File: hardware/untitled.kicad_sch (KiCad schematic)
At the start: 41 parts, among them J5 DCJ200-10-A-K1-K, J6 USB4105-GF-A, SW1 SW_Push, SW2 SW_Push, U3 NCP1117ST33T3G, U4 ESP32-S3-WROOM-1-N8R8, U5 USBLC6-2SC6

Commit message: SD card routing v0.1
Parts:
- removed R23: 50R, Resistor_SMD:R_0603_1608Metric_Pad0.98x0.95mm_HandSolder, symbol Device:R
- SW1: renamed from S1; footprint R1966ABLKBLKGR -> ESP32-project-footprints:RA1113112R
- renumbered R15 to R17, R16 to R18, R17 to R19, R18 to R20, R19 to R21, R20 to R22, R21 to R23, R22 to R24, R24 to R25, R25 to R26, SW1 to SW2, SW2 to SW3
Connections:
- net +5V: no longer C19.1
- net SPI2_MISO: now also U4.21 (IO13)
- net VBUS: now also C19.1
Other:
- note removed: "NEW SWITCH"
- moved on the sheet: C19, U5

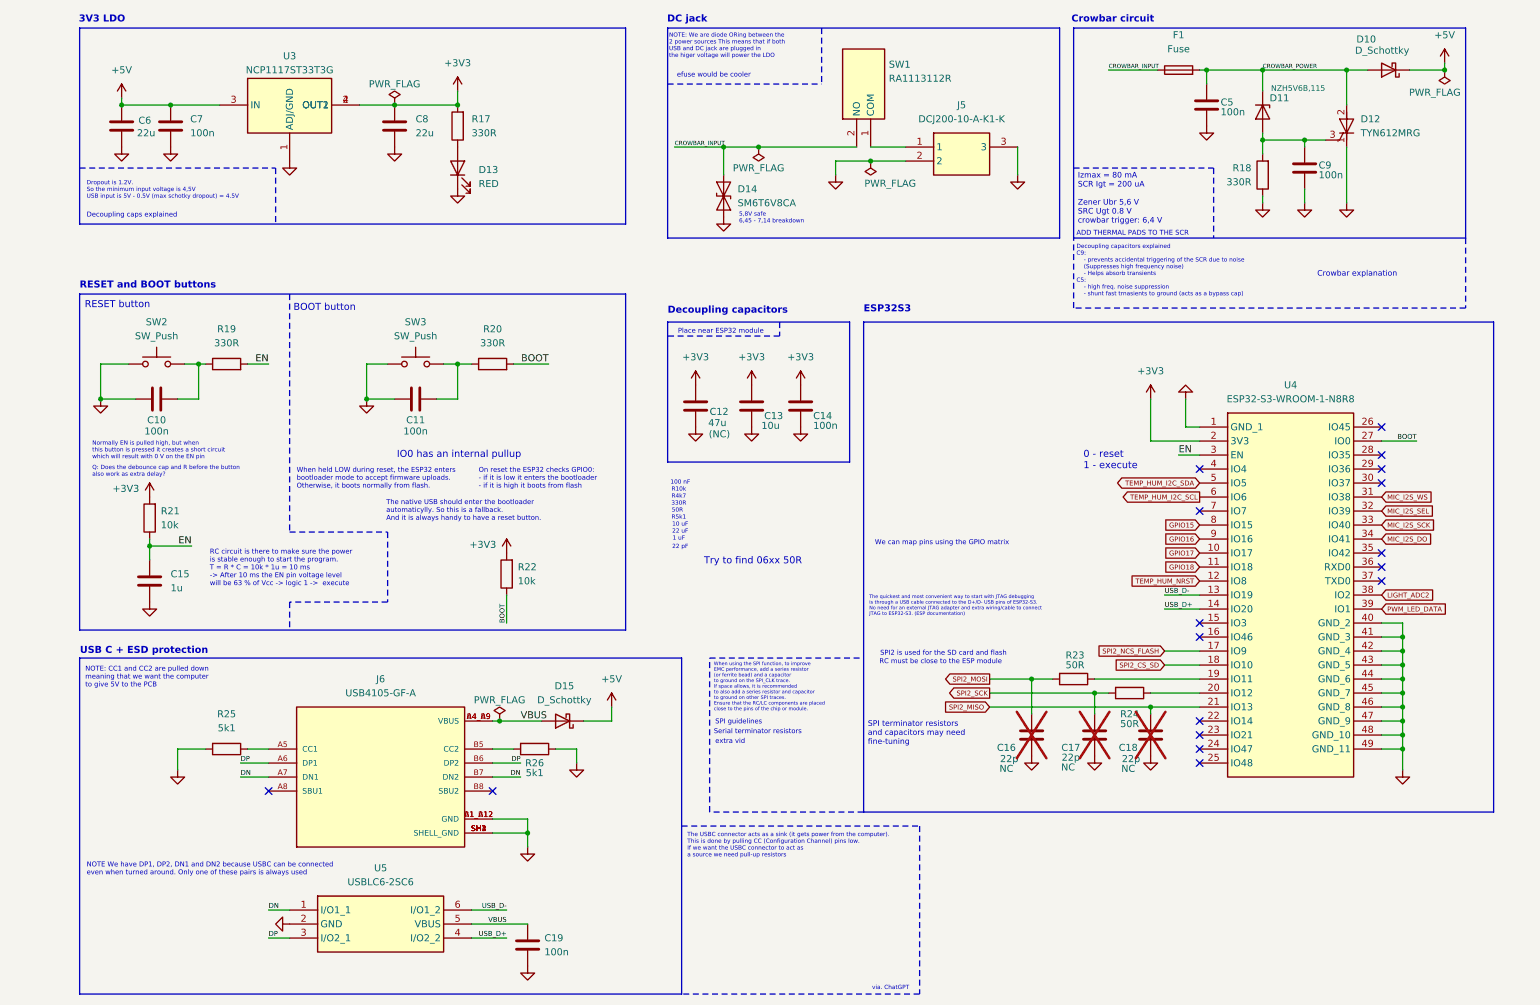
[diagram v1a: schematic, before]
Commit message: v0.3.1 Changed board stackup and impedance controlled traces
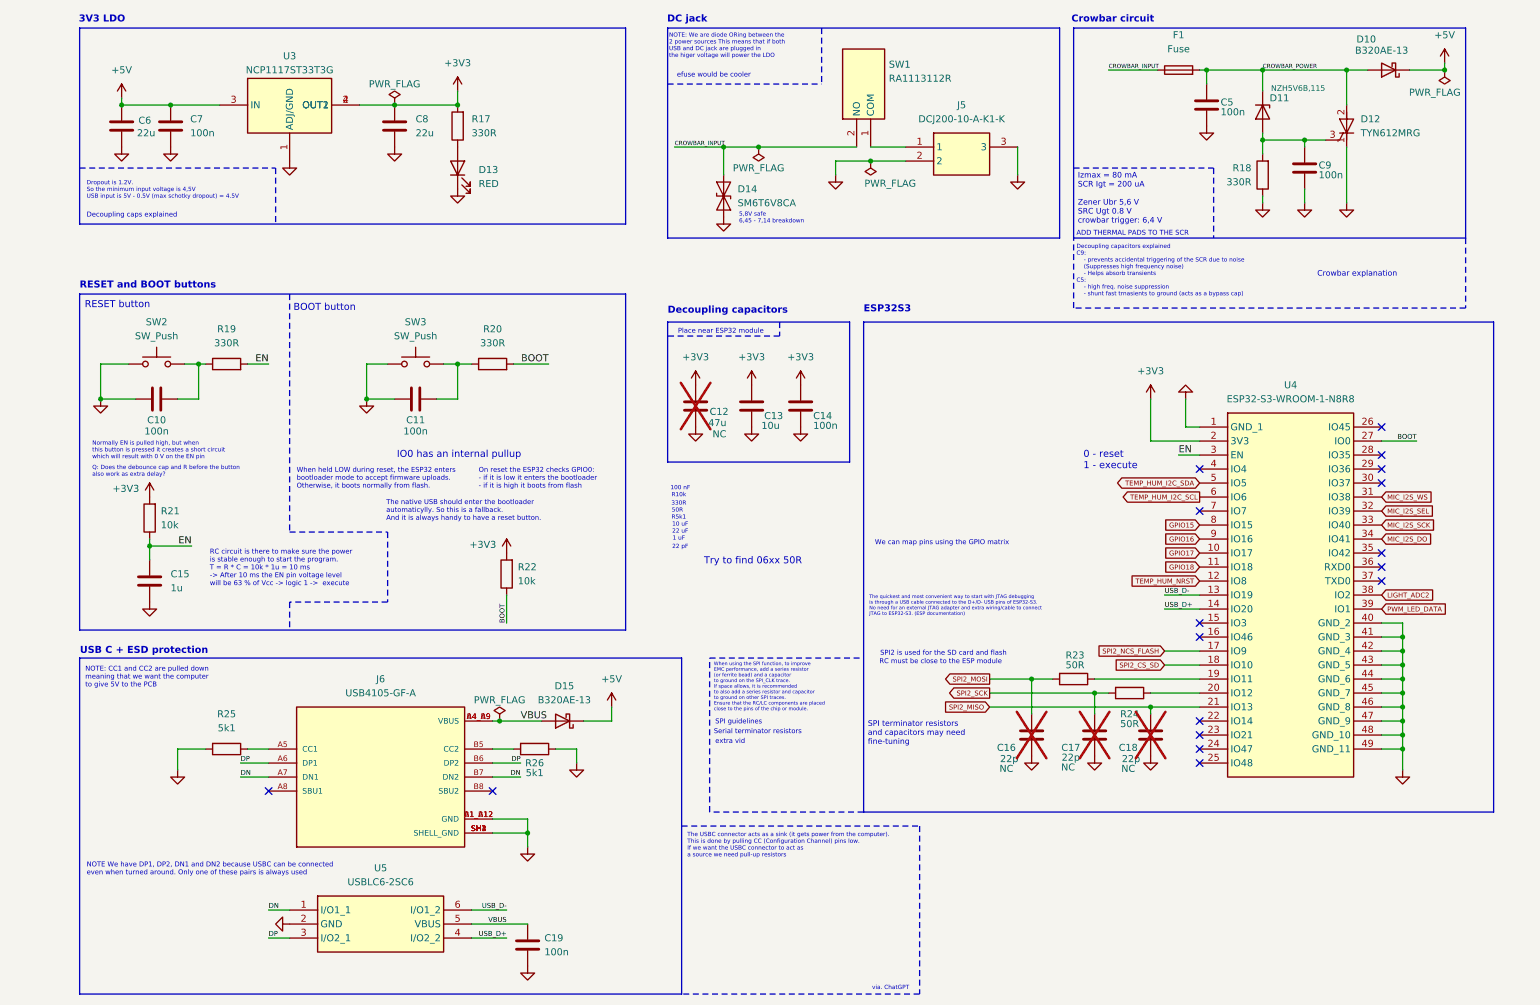
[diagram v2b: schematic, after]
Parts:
- C12: Note (NC) -> NC; now not fitted
- D10, D15: value D_Schottky -> B320AE-13
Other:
- note removed: "R4k7"
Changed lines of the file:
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@@
 	(text "R10k"
 		(exclude_from_sim no)
-		(at 131.572 104.14 0)
+		(at 131.572 105.156 0)
 		(effects
 			(font
@@
 		)
 	)
-	(text "R4k7"
-		(exclude_from_sim no)
-		(at 131.572 105.41 0)
-		(effects
-			(font
-				(size 0.762 0.762)
-				(color 39 255 0 1)
-			)
-			(href "https://www.tme.eu/cz/details/rc0603fr-074k7/rezistory-smd/yageo/rc0603fr-074k7l/")
-		)
-	)
 	(text "0 - reset\n1 - execute"
 		(exclude_from_sim no)
@@
 	(text "100 nF"
 		(exclude_from_sim no)
-		(at 130.048 102.87 0)
+		(at 130.048 103.886 0)
 		(effects
 			(font
@@
 			)
 		)
-		(property "Value" "D_Schottky"
+		(property "Value" "B320AE-13"
 			(at 110.8075 142.24 0)
 			(effects
@@
 			)
 		)
-		(property "Value" "D_Schottky"
+		(property "Value" "B320AE-13"
 			(at 254.254 24.384 0)
 			(effects
@@
 		(in_bom yes)
 		(on_board yes)
-		(dnp no)
+		(dnp yes)
 		(property "Reference" "C12"
 			(at 137.16 89.916 0)
@@
 			)
 		)
-		(property "Note" "(NC)"
+		(property "Note" "NC"
 			(at 138.938 93.98 0)
 			(effects

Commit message: Working prototype, PCB prototype revision done
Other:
- note added: "50 OMHS RES SHOULD HAVE 0402 FOOTPRINT"
- note added: "ADD GPIO3 PULLUP/DOWN SWITCH AND BURN FUSE EFUSE_STRAP_JTAG_SEL"
- note added: "ADD PINS FOR JTAG AND PROGRAM (RX, TX, EN, IO0, MTDI, MTDO, MTCLK, MTMS, GPIO3, 3,3V, GND)"
- note added: "BOOT CIRCUITARY WORKS WITHOUT C15"
- note added: "DECOUPLING WORKS WITHOUT C12"
- note added: "WORKS"
- note added: "WORKS EVEN WHEN BOTH USB AND DC JACK IS PLUGGED IN"
- note added: "WORKS FOR POWER BUT NOT FOR DEBUGGING ISNT RECOGNIZED AS A SERIAL PORT"
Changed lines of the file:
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@@
+		)
+	)
+	(text "ADD GPIO3 PULLUP/DOWN SWITCH\nAND BURN FUSE EFUSE_STRAP_JTAG_SEL"
+		(exclude_from_sim no)
+		(at 186.436 80.264 0)
+		(effects
+			(font
+				(size 1.27 1.27)
+				(color 0 255 10 1)
+			)
 		)
 	)
@@
 		)
 	)
+	(text "WORKS"
+		(exclude_from_sim no)
+		(at 27.686 23.622 0)
+		(effects
+			(font
+				(size 1.27 1.27)
+				(color 10 255 0 1)
+			)
+		)
+	)
+	(text "DECOUPLING WORKS WITHOUT C12"
+		(exclude_from_sim no)
+		(at 145.288 100.838 0)
+		(effects
+			(font
+				(size 1.27 1.27)
+				(color 0 255 10 1)
+			)
+		)
+	)
 	(text "Crowbar explanation"
 		(exclude_from_sim no)
@@
 			)
 			(justify left)
-			(href "https://www.tme.eu/cz/details/08051c104j4t2a/kondenzatory-mlcc-smd/kyocera-avx/")
+			(href "https://www.tme.eu/cz/details/cl21b104kbcnnnc/kondenzatory-mlcc-smd/samsung/")
 		)
 	)
@@
 		)
 	)
+	(text "50 OMHS RES SHOULD HAVE\n0402 FOOTPRINT"
+		(exclude_from_sim no)
+		(at 181.102 95.504 0)
+		(effects
+			(font
+				(size 1.27 1.27)
+				(color 0 255 10 1)
+			)
+		)
+	)
 	(text "When held LOW during reset, the ESP32 enters \nbootloader mode to accept firmware uploads.\nOtherwise, it boots normally from flash."
 		(exclude_from_sim no)
@@
 			(justify left)
 			(href "https://www.youtube.com/watch?v=X71YDKgRJvA")
+		)
+	)
+	(text "WORKS FOR POWER BUT NOT FOR DEBUGGING\nISNT RECOGNIZED AS A SERIAL PORT"
+		(exclude_from_sim no)
+		(at 35.56 166.624 0)
+		(effects
+			(font
+				(size 1.27 1.27)
+				(color 19 255 0 1)
+			)
 		)
 	)
@@
 		)
 	)
+	(text "ADD PINS FOR JTAG AND PROGRAM \n(RX, TX, EN, IO0, MTDI, MTDO, MTCLK,\nMTMS, GPIO3, 3,3V, GND)"
+		(exclude_from_sim no)
+		(at 185.42 88.138 0)
+		(effects
+			(font
+				(size 1.27 1.27)
+				(color 0 255 10 1)
+			)
+		)
+	)
+	(text "BOOT CIRCUITARY WORKS WITHOUT C15"
+		(exclude_from_sim no)
+		(at 62.738 127 0)
+		(effects
+			(font
+				(size 1.27 1.27)
+				(color 19 255 0 1)
+			)
+		)
+	)
 	(text "NOTE We have DP1, DP2, DN1 and DN2 because USBC can be connected\neven when turned around. Only one of these pairs is always used"
 		(exclude_from_sim no)
@@
 		)
 	)
+	(text "WORKS"
+		(exclude_from_sim no)
+		(at 138.176 34.544 0)
+		(effects
+			(font
+				(size 1.27 1.27)
+				(color 44 255 4 1)
+			)
+		)
+	)
+	(text "WORKS\nEVEN WHEN BOTH USB\nAND DC JACK IS PLUGGED IN"
+		(exclude_from_sim no)
+		(at 269.494 47.752 0)
+		(effects
+			(font
+				(size 1.27 1.27)
+				(color 0 255 10 1)
+			)
+		)
+	)

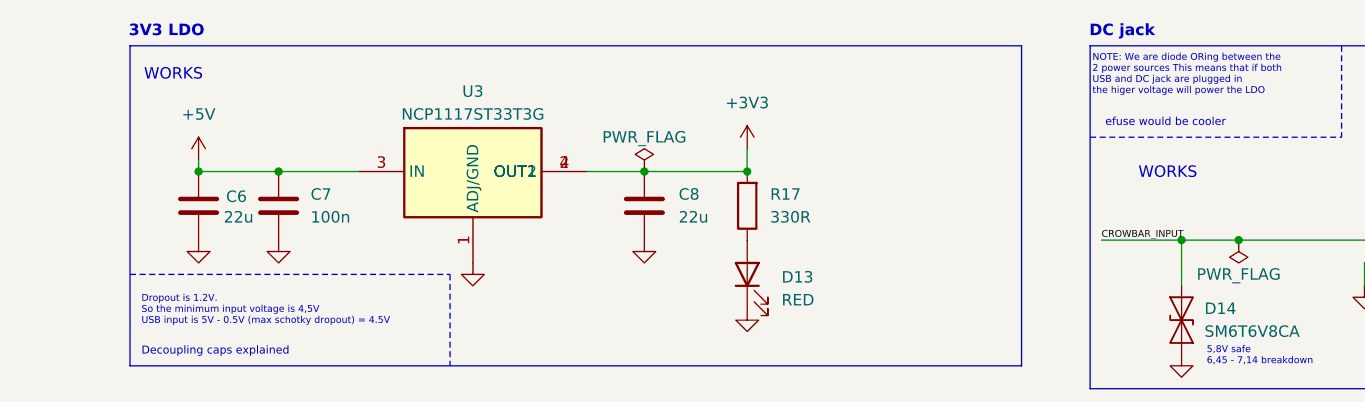
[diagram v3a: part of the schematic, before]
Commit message: pcb file is broken
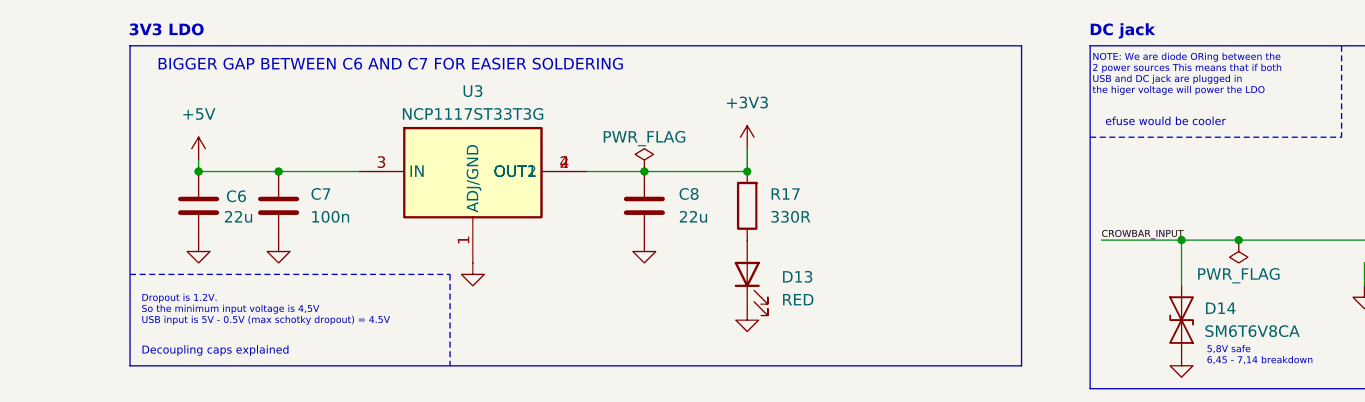
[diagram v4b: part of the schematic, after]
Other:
- note added: "BIGGER GAP BETWEEN C6 AND C7 FOR EASIER SOLDERING"
- note removed: "WORKS"
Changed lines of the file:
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@@
 				(thickness 0.254)
 				(bold yes)
+				(color 255 0 6 1)
 			)
 		)
@@
 				(thickness 0.254)
 				(bold yes)
+				(color 255 0 7 1)
+			)
+		)
+	)
+	(text "BIGGER GAP BETWEEN C6 AND C7 FOR EASIER SOLDERING"
+		(exclude_from_sim no)
+		(at 51.816 22.606 0)
+		(effects
+			(font
+				(size 1.27 1.27)
 			)
 		)
@@
 			)
 			(justify left)
-		)
-	)
-	(text "WORKS"
-		(exclude_from_sim no)
-		(at 27.686 23.622 0)
-		(effects
-			(font
-				(size 1.27 1.27)
-				(color 10 255 0 1)
-			)
 		)
 	)
@@
 				(thickness 0.254)
 				(bold yes)
+				(color 255 6 19 1)
 			)
 		)
@@
 		)
 	)
-	(text "WORKS"
-		(exclude_from_sim no)
-		(at 138.176 34.544 0)
-		(effects
-			(font
-				(size 1.27 1.27)
-				(color 44 255 4 1)
-			)
-		)
-	)
